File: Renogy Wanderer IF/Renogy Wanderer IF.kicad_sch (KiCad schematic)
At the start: 3 parts

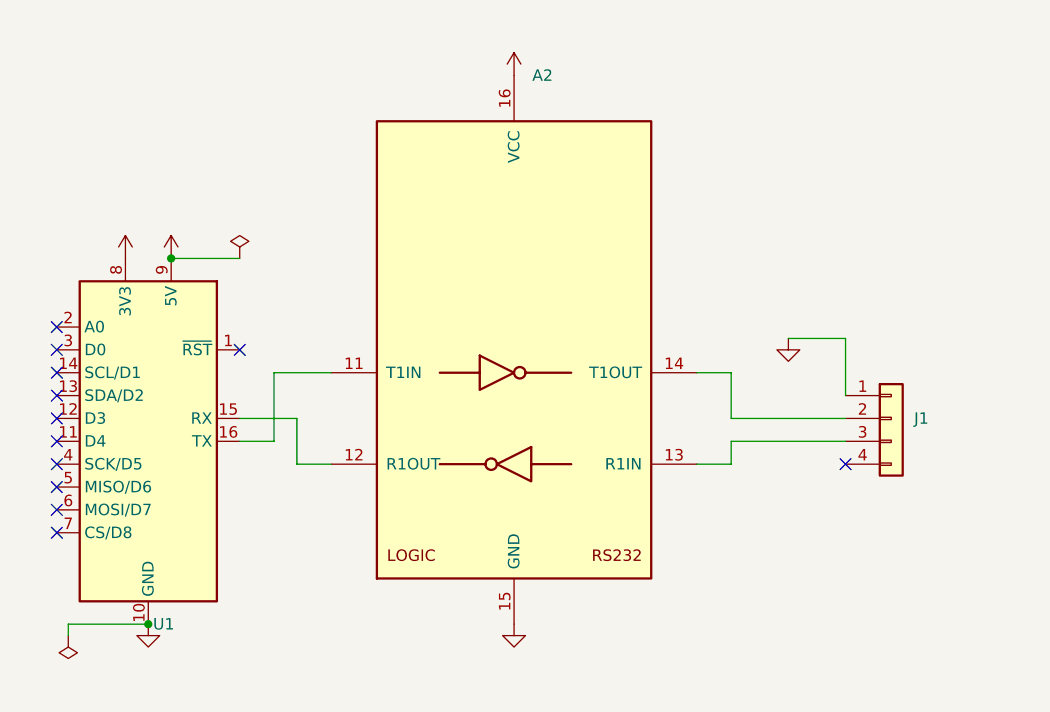
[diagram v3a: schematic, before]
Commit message: Add wake from sleep
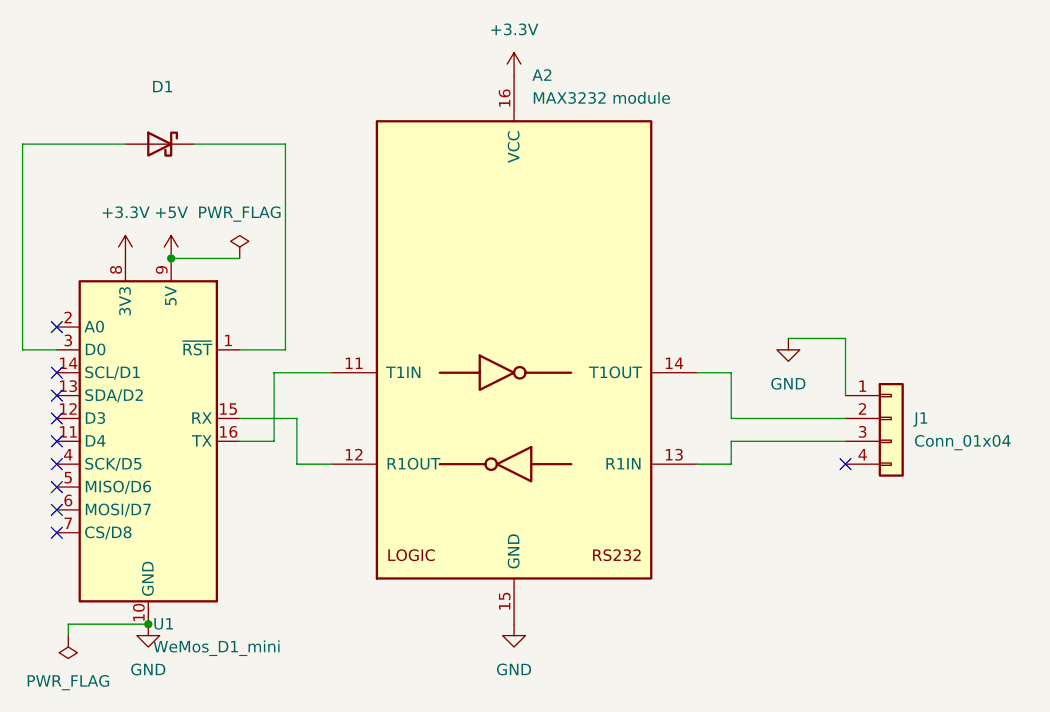
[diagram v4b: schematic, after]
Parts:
- added D1: (no value), symbol Device:D_Schottky
- A2: value (none) -> MAX3232 module; footprint (none) -> Module:MAX3232 module
- J1: value (none) -> Conn_01x04; footprint (none) -> Connector_Wire:SolderWire-0.1sqmm_1x04_P3.6mm_D0.4mm_OD1mm
- U1: value (none) -> WeMos_D1_mini; footprint (none) -> Module:WEMOS_D1_mini_light
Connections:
- net at U1.1 (~{RST}): now also D1.1 (K)
- net at U1.3 (D0): now also D1.2 (A)
- no-connect marks 12 -> 10
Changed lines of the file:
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@@
   )
   (no_connect (at 125.73 83.82))
-  (no_connect (at 146.05 86.36))
   (no_connect (at 125.73 93.98))
   (no_connect (at 125.73 96.52))
@@
   (no_connect (at 125.73 104.14))
   (no_connect (at 213.36 99.06))
-  (no_connect (at 125.73 86.36))
   (wire (pts (xy 200.66 93.98) (xy 213.36 93.98))
     (stroke (width 0) (type default) (color 0 0 0 0))
@@
     (stroke (width 0) (type default) (color 0 0 0 0))
   )
+  (wire (pts (xy 146.05 86.36) (xy 151.13 86.36))
+    (stroke (width 0) (type default) (color 0 0 0 0))
+  )
+  (wire (pts (xy 133.35 63.5) (xy 121.92 63.5))
+    (stroke (width 0) (type default) (color 0 0 0 0))
+  )
   (wire (pts (xy 127 118.11) (xy 127 116.84))
     (stroke (width 0) (type default) (color 0 0 0 0))
@@
     (stroke (width 0) (type default) (color 0 0 0 0))
   )
+  (wire (pts (xy 140.97 63.5) (xy 151.13 63.5))
+    (stroke (width 0) (type default) (color 0 0 0 0))
+  )
   (wire (pts (xy 196.85 88.9) (xy 200.66 88.9))
     (stroke (width 0) (type default) (color 0 0 0 0))
@@
     (stroke (width 0) (type default) (color 0 0 0 0))
   )
+  (wire (pts (xy 121.92 63.5) (xy 121.92 86.36))
+    (stroke (width 0) (type default) (color 0 0 0 0))
+  )
+  (wire (pts (xy 151.13 63.5) (xy 151.13 86.36))
+    (stroke (width 0) (type default) (color 0 0 0 0))
+  )
   (wire (pts (xy 149.86 88.9) (xy 149.86 96.52))
     (stroke (width 0) (type default) (color 0 0 0 0))
@@
     (stroke (width 0) (type default) (color 0 0 0 0))
   )
+  (wire (pts (xy 121.92 86.36) (xy 125.73 86.36))
+    (stroke (width 0) (type default) (color 0 0 0 0))
+  )
   (wire (pts (xy 156.21 88.9) (xy 149.86 88.9))
     (stroke (width 0) (type default) (color 0 0 0 0))
@@
       (effects (font (size 1.27 1.27)) hide)
     )
-    (property "Value" "" (id 1) (at 133.35 71.12 0))
+    (property "Value" "+3.3V" (id 1) (at 133.35 71.12 0))
     (property "Footprint" "" (id 2) (at 133.35 76.2 0)
       (effects (font (size 1.27 1.27)) hide)
@@
       (effects (font (size 1.27 1.27)) hide)
     )
-    (property "Value" "" (id 1) (at 146.05 71.12 0))
+    (property "Value" "PWR_FLAG" (id 1) (at 146.05 71.12 0))
     (property "Footprint" "" (id 2) (at 146.05 76.2 0)
       (effects (font (size 1.27 1.27)) hide)
@@
     )
     (pin "1")
+  )
+  (symbol (lib_id "Device:D_Schottky") (at 137.16 63.5 0) (mirror y) (unit 1)
+    (in_bom yes) (on_board yes) (fields_autoplaced)
+    (property "Reference" "D1" (id 0) (at 137.4775 57.15 0))
+    (property "Value" "" (id 1) (at 137.4775 59.69 0))
+    (property "Footprint" "" (id 2) (at 137.16 63.5 0)
+      (effects (font (size 1.27 1.27)) hide)
+    )
+    (property "Datasheet" "~" (id 3) (at 137.16 63.5 0)
+      (effects (font (size 1.27 1.27)) hide)
+    )
+    (pin "1")
+    (pin "2")
   )
   (symbol (lib_id "MCU_Module:WeMos_D1_mini") (at 135.89 96.52 0) (mirror y) (unit 1)
@@
       (effects (font (size 1.27 1.27)) (justify right))
     )
-    (property "Value" "" (id 1) (at 136.4106 119.38 0)
+    (property "Value" "WeMos_D1_mini" (id 1) (at 136.4106 119.38 0)
       (effects (font (size 1.27 1.27)) (justify right))
     )
-    (property "Footprint" "" (id 2) (at 135.89 125.73 0)
+    (property "Footprint" "Module:WEMOS_D1_mini_light" (id 2) (at 135.89 125.73 0)
       (effects (font (size 1.27 1.27)) hide)
     )
@@
       (effects (font (size 1.27 1.27)) hide)
     )
-    (property "Value" "" (id 1) (at 207.01 90.17 0))
+    (property "Value" "GND" (id 1) (at 207.01 90.17 0))
     (property "Footprint" "" (id 2) (at 207.01 85.09 0)
       (effects (font (size 1.27 1.27)) hide)
@@
       (effects (font (size 1.27 1.27)) hide)
     )
-    (property "Value" "" (id 1) (at 135.89 121.92 0))
+    (property "Value" "GND" (id 1) (at 135.89 121.92 0))
     (property "Footprint" "" (id 2) (at 135.89 116.84 0)
       (effects (font (size 1.27 1.27)) hide)
@@
       (effects (font (size 1.27 1.27)) (justify left))
     )
-    (property "Value" "" (id 1) (at 220.98 96.5199 0)
+    (property "Value" "Conn_01x04" (id 1) (at 220.98 96.5199 0)
       (effects (font (size 1.27 1.27)) (justify left))
     )
-    (property "Footprint" "" (id 2) (at 218.44 93.98 0)
+    (property "Footprint" "Connector_Wire:SolderWire-0.1sqmm_1x04_P3.6mm_D0.4mm_OD1mm" (id 2) (at 218.44 93.98 0)
       (effects (font (size 1.27 1.27)) hide)
     )
@@
       (effects (font (size 1.27 1.27)) hide)
     )
-    (property "Value" "" (id 1) (at 138.43 71.12 0))
+    (property "Value" "+5V" (id 1) (at 138.43 71.12 0))
     (property "Footprint" "" (id 2) (at 138.43 76.2 0)
       (effects (font (size 1.27 1.27)) hide)
@@
       (effects (font (size 1.27 1.27)) (justify left))
     )
-    (property "Value" "" (id 1) (at 178.5494 58.42 0)
+    (property "Value" "MAX3232 module" (id 1) (at 178.5494 58.42 0)
       (effects (font (size 1.27 1.27)) (justify left))
     )
-    (property "Footprint" "" (id 2) (at 177.8 113.03 0)
+    (property "Footprint" "Module:MAX3232 module" (id 2) (at 177.8 113.03 0)
       (effects (font (size 1.27 1.27)) (justify left) hide)
     )
@@
       (effects (font (size 1.27 1.27)) hide)
     )
-    (property "Value" "" (id 1) (at 176.53 50.8 0))
+    (property "Value" "+3.3V" (id 1) (at 176.53 50.8 0))
     (property "Footprint" "" (id 2) (at 176.53 55.88 0)
       (effects (font (size 1.27 1.27)) hide)
@@
       (effects (font (size 1.27 1.27)) hide)
     )
-    (property "Value" "" (id 1) (at 127 123.19 0))
+    (property "Value" "PWR_FLAG" (id 1) (at 127 123.19 0))
     (property "Footprint" "" (id 2) (at 127 118.11 0)
       (effects (font (size 1.27 1.27)) hide)
@@
       (effects (font (size 1.27 1.27)) hide)
     )
-    (property "Value" "" (id 1) (at 176.53 121.92 0))
+    (property "Value" "GND" (id 1) (at 176.53 121.92 0))
     (property "Footprint" "" (id 2) (at 176.53 116.84 0)
       (effects (font (size 1.27 1.27)) hide)
@@
       (reference "A2") (unit 1) (value "MAX3232 module") (footprint "Module:MAX3232 module")
     )
+    (path "/4736f749-4a0e-4a05-b1aa-d51f1c3fc23d"
+      (reference "D1") (unit 1) (value "D_Schottky") (footprint "Diode_THT:D_DO-201_P15.24mm_Horizontal")
+    )
     (path "/c0ff5ddf-dec1-4710-89a0-57f597d38d9f"

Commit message: Invert the RS232 module for easier mounting
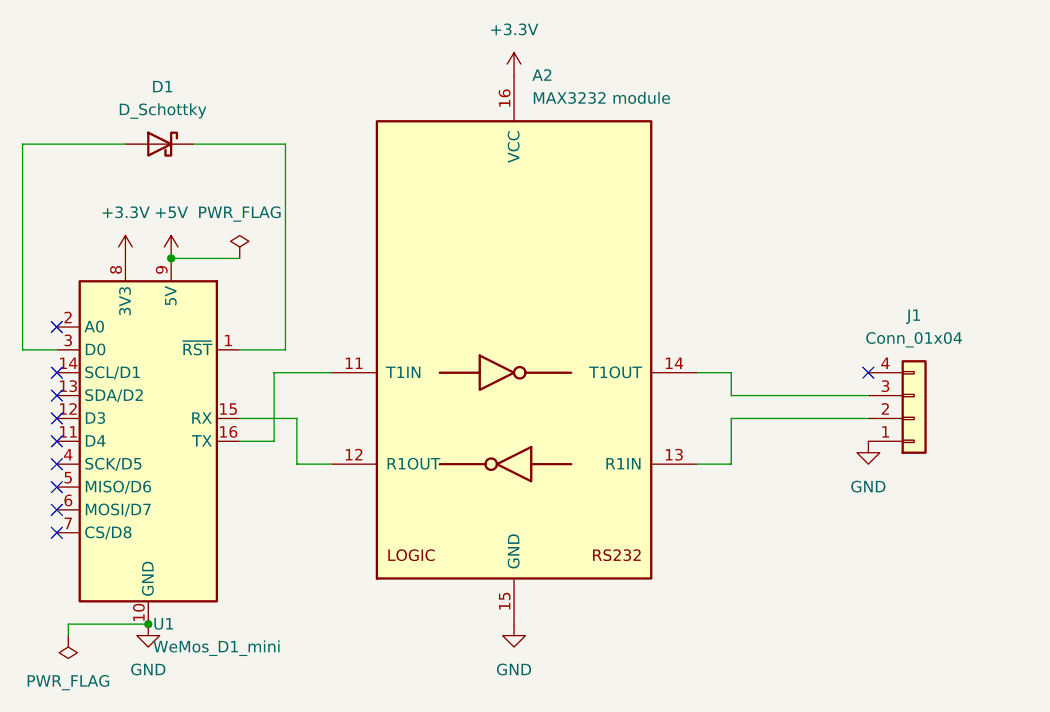
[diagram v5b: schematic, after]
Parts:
- A2: footprint Module:MAX3232 module -> (none)
- D1: value (none) -> D_Schottky
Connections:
- net at J1.2 (Pin_2): now also A2.13 (R1IN); no longer A2.14 (T1OUT)
- net at J1.3 (Pin_3): now also A2.14 (T1OUT); no longer A2.13 (R1IN)
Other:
- moved on the sheet: J1
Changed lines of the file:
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@@
   (no_connect (at 125.73 99.06))
   (no_connect (at 125.73 104.14))
-  (no_connect (at 213.36 99.06))
-  (wire (pts (xy 200.66 93.98) (xy 213.36 93.98))
+  (no_connect (at 215.9 88.9))
+  (wire (pts (xy 200.66 91.44) (xy 215.9 91.44))
     (stroke (width 0) (type default) (color 0 0 0 0))
   )
@@
     (stroke (width 0) (type default) (color 0 0 0 0))
   )
-  (wire (pts (xy 200.66 99.06) (xy 200.66 96.52))
+  (wire (pts (xy 200.66 99.06) (xy 200.66 93.98))
     (stroke (width 0) (type default) (color 0 0 0 0))
   )
@@
     (stroke (width 0) (type default) (color 0 0 0 0))
   )
-  (wire (pts (xy 200.66 96.52) (xy 213.36 96.52))
+  (wire (pts (xy 200.66 93.98) (xy 215.9 93.98))
     (stroke (width 0) (type default) (color 0 0 0 0))
   )
@@
     (stroke (width 0) (type default) (color 0 0 0 0))
   )
-  (wire (pts (xy 213.36 85.09) (xy 207.01 85.09))
-    (stroke (width 0) (type default) (color 0 0 0 0))
-  )
-  (wire (pts (xy 213.36 91.44) (xy 213.36 85.09))
-    (stroke (width 0) (type default) (color 0 0 0 0))
-  )
-  (wire (pts (xy 200.66 88.9) (xy 200.66 93.98))
+  (wire (pts (xy 200.66 88.9) (xy 200.66 91.44))
     (stroke (width 0) (type default) (color 0 0 0 0))
   )
@@
     (in_bom yes) (on_board yes) (fields_autoplaced)
     (property "Reference" "D1" (id 0) (at 137.4775 57.15 0))
-    (property "Value" "" (id 1) (at 137.4775 59.69 0))
+    (property "Value" "D_Schottky" (id 1) (at 137.4775 59.69 0))
     (property "Footprint" "" (id 2) (at 137.16 63.5 0)
       (effects (font (size 1.27 1.27)) hide)
@@
     (pin "9")
   )
-  (symbol (lib_id "power:GND") (at 207.01 85.09 0) (unit 1)
-    (in_bom yes) (on_board yes) (fields_autoplaced)
-    (property "Reference" "#PWR03" (id 0) (at 207.01 91.44 0)
-      (effects (font (size 1.27 1.27)) hide)
-    )
-    (property "Value" "GND" (id 1) (at 207.01 90.17 0))
-    (property "Footprint" "" (id 2) (at 207.01 85.09 0)
-      (effects (font (size 1.27 1.27)) hide)
-    )
-    (property "Datasheet" "" (id 3) (at 207.01 85.09 0)
+  (symbol (lib_id "power:GND") (at 215.9 96.52 0) (unit 1)
+    (in_bom yes) (on_board yes) (fields_autoplaced)
+    (property "Reference" "#PWR03" (id 0) (at 215.9 102.87 0)
+      (effects (font (size 1.27 1.27)) hide)
+    )
+    (property "Value" "GND" (id 1) (at 215.9 101.6 0))
+    (property "Footprint" "" (id 2) (at 215.9 96.52 0)
+      (effects (font (size 1.27 1.27)) hide)
+    )
+    (property "Datasheet" "" (id 3) (at 215.9 96.52 0)
       (effects (font (size 1.27 1.27)) hide)
     )
@@
     (pin "1")
   )
-  (symbol (lib_id "Connector_Generic:Conn_01x04") (at 218.44 93.98 0) (unit 1)
-    (in_bom yes) (on_board yes) (fields_autoplaced)
-    (property "Reference" "J1" (id 0) (at 220.98 93.9799 0)
-      (effects (font (size 1.27 1.27)) (justify left))
-    )
-    (property "Value" "Conn_01x04" (id 1) (at 220.98 96.5199 0)
-      (effects (font (size 1.27 1.27)) (justify left))
-    )
-    (property "Footprint" "Connector_Wire:SolderWire-0.1sqmm_1x04_P3.6mm_D0.4mm_OD1mm" (id 2) (at 218.44 93.98 0)
-      (effects (font (size 1.27 1.27)) hide)
-    )
-    (property "Datasheet" "~" (id 3) (at 218.44 93.98 0)
+  (symbol (lib_id "Connector_Generic:Conn_01x04") (at 220.98 93.98 0) (mirror x) (unit 1)
+    (in_bom yes) (on_board yes) (fields_autoplaced)
+    (property "Reference" "J1" (id 0) (at 220.98 82.55 0))
+    (property "Value" "Conn_01x04" (id 1) (at 220.98 85.09 0))
+    (property "Footprint" "Connector_Wire:SolderWire-0.1sqmm_1x04_P3.6mm_D0.4mm_OD1mm" (id 2) (at 220.98 93.98 0)
+      (effects (font (size 1.27 1.27)) hide)
+    )
+    (property "Datasheet" "~" (id 3) (at 220.98 93.98 0)
       (effects (font (size 1.27 1.27)) hide)
     )
@@
       (effects (font (size 1.27 1.27)) (justify left))
     )
-    (property "Footprint" "Module:MAX3232 module" (id 2) (at 177.8 113.03 0)
+    (property "Footprint" "" (id 2) (at 177.8 113.03 0)
       (effects (font (size 1.27 1.27)) (justify left) hide)
     )
@@
     )
     (path "/da01b3e4-26f2-4f90-b4fe-3db1c5dc3840"
-      (reference "A2") (unit 1) (value "MAX3232 module") (footprint "Module:MAX3232 module")
+      (reference "A2") (unit 1) (value "MAX3232 module") (footprint "Module:MAX3232 module inverted")
     )
     (path "/4736f749-4a0e-4a05-b1aa-d51f1c3fc23d"
-      (reference "D1") (unit 1) (value "D_Schottky") (footprint "Diode_THT:D_DO-201_P15.24mm_Horizontal")
+      (reference "D1") (unit 1) (value "D_Schottky") (footprint "Diode_THT:D_DO-34_SOD68_P10.16mm_Horizontal")
     )
     (path "/c0ff5ddf-dec1-4710-89a0-57f597d38d9f"
